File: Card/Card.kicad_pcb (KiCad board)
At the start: 2 copper layers, 89 x 51 mm, 4 parts

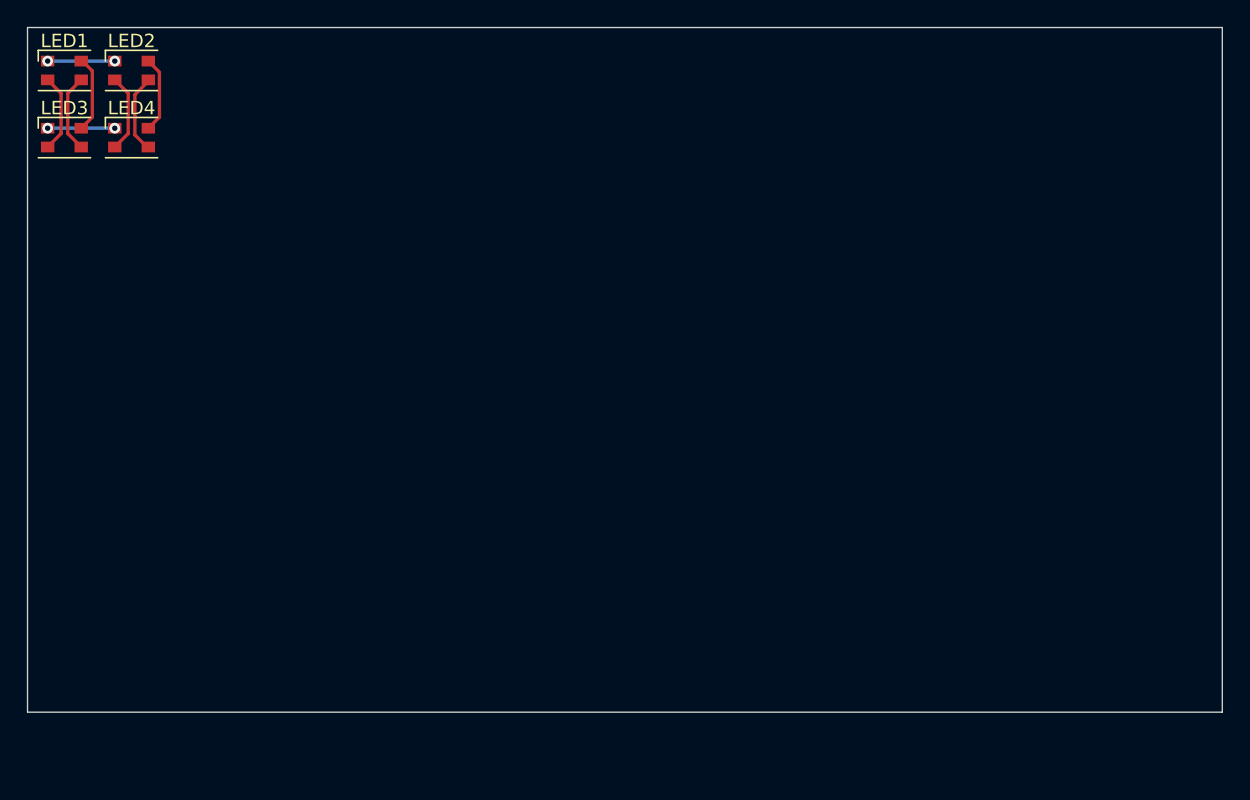
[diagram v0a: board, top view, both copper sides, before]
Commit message: Updated to UK card size
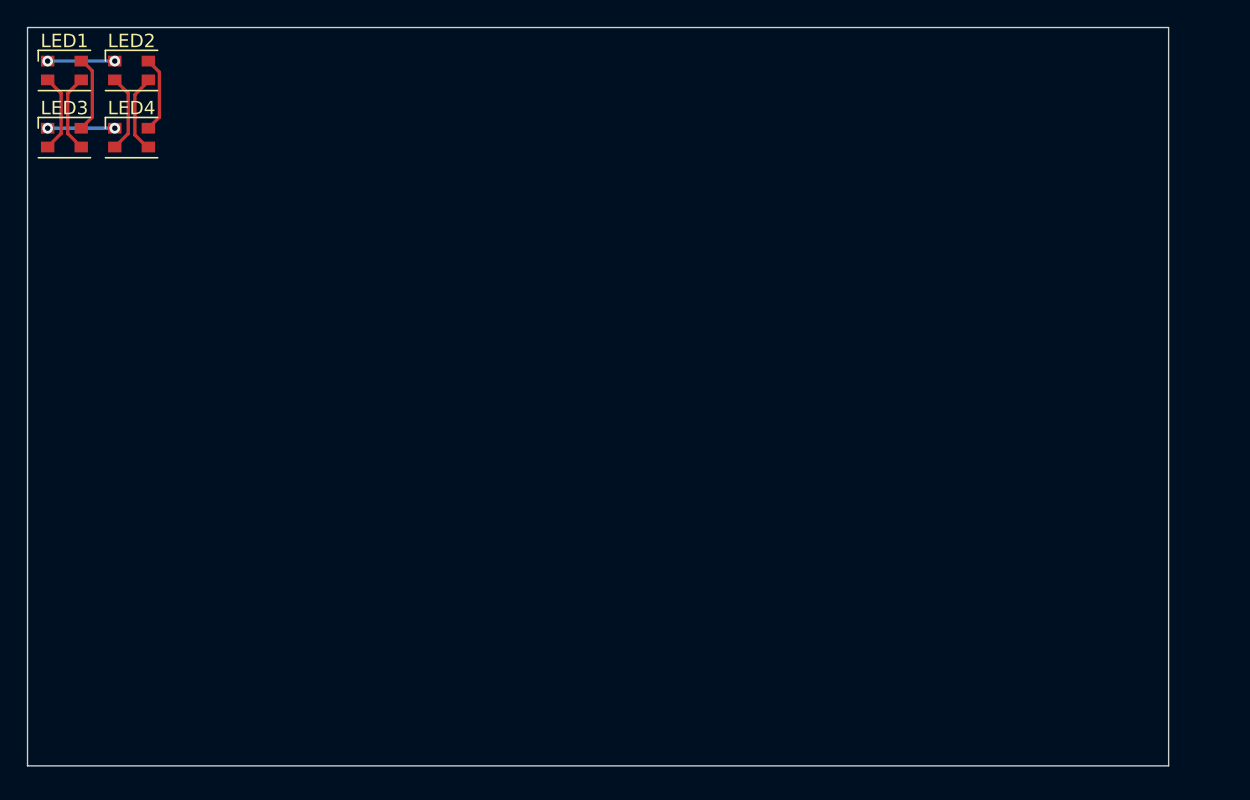
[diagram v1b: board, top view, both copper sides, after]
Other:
- board size 89 x 51 mm -> 85 x 55 mm
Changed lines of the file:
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@@
     )
   )
-  (gr_rect (start 100.5 61.5) (end 189.5 112.5)
+  (gr_rect (start 100.5 61.5) (end 185.5 116.5)
     (stroke (width 0.1) (type default)) (fill none) (layer "Edge.Cuts"))
   (via (at 107 64) (size 0.8) (drill 0.4) (layers "F.Cu" "B.Cu") (net 1))

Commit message: created LED matrix
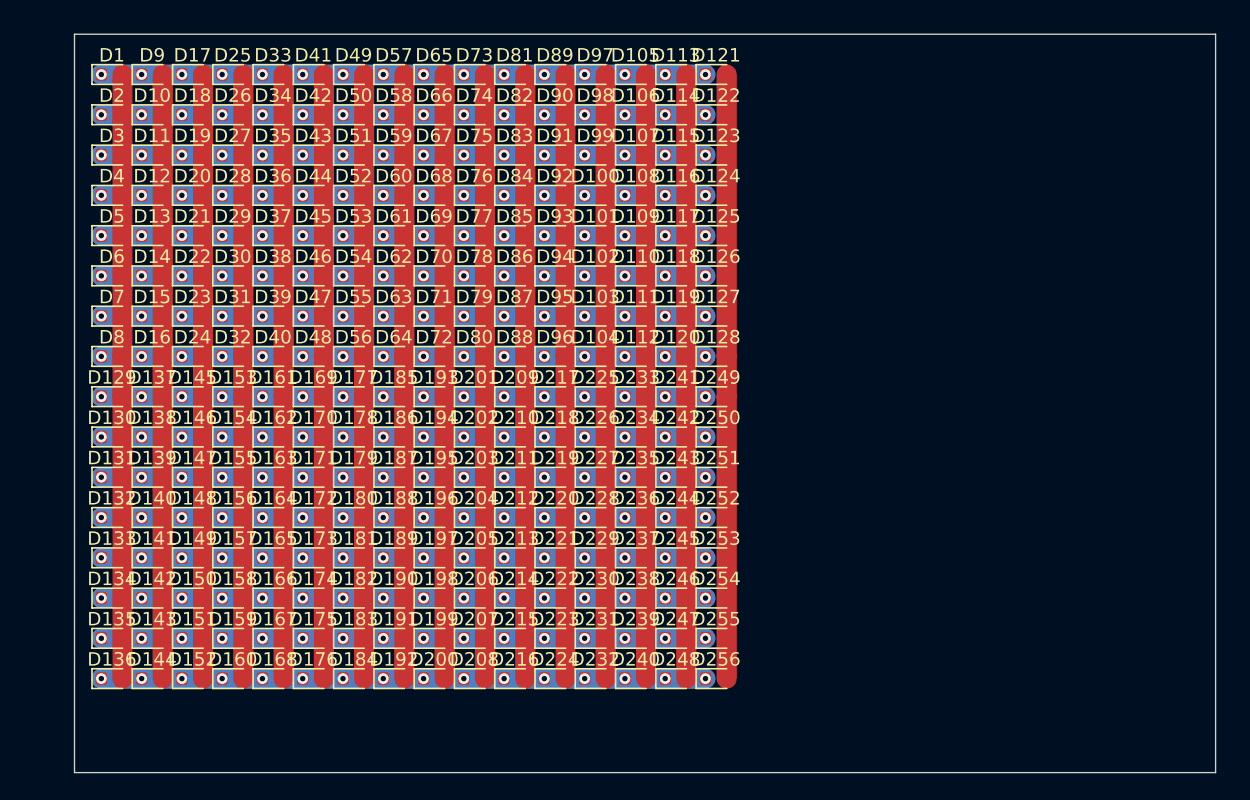
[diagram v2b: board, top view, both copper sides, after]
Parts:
- removed LED1, LED2, LED3, LED4: Tri-LED_CA, Footprints:LED_Cree-PLCC4_3.2x2.8mm_CCW
- added D1: LED, LED_SMD:LED_0603_1608Metric, F.Cu at (106.8, 65.0)
- added D10: LED, LED_SMD:LED_0603_1608Metric, F.Cu at (109.8, 68.0)
- added D100: LED, LED_SMD:LED_0603_1608Metric, F.Cu at (142.8, 74.0)
- added D101: LED, LED_SMD:LED_0603_1608Metric, F.Cu at (142.8, 77.0)
- added D102: LED, LED_SMD:LED_0603_1608Metric, F.Cu at (142.8, 80.0)
- added D103: LED, LED_SMD:LED_0603_1608Metric, F.Cu at (142.8, 83.0)
- added D104: LED, LED_SMD:LED_0603_1608Metric, F.Cu at (142.8, 86.0)
- added D105: LED, LED_SMD:LED_0603_1608Metric, F.Cu at (145.8, 65.0)
- added D106: LED, LED_SMD:LED_0603_1608Metric, F.Cu at (145.8, 68.0)
- added D107: LED, LED_SMD:LED_0603_1608Metric, F.Cu at (145.8, 71.0)
- added D108: LED, LED_SMD:LED_0603_1608Metric, F.Cu at (145.8, 74.0)
- added D109: LED, LED_SMD:LED_0603_1608Metric, F.Cu at (145.8, 77.0)
- added D11: LED, LED_SMD:LED_0603_1608Metric, F.Cu at (109.8, 71.0)
- added D110: LED, LED_SMD:LED_0603_1608Metric, F.Cu at (145.8, 80.0)
- added D111: LED, LED_SMD:LED_0603_1608Metric, F.Cu at (145.8, 83.0)
- added D112: LED, LED_SMD:LED_0603_1608Metric, F.Cu at (145.8, 86.0)
- added D113: LED, LED_SMD:LED_0603_1608Metric, F.Cu at (148.8, 65.0)
- added D114: LED, LED_SMD:LED_0603_1608Metric, F.Cu at (148.8, 68.0)
- added D115: LED, LED_SMD:LED_0603_1608Metric, F.Cu at (148.8, 71.0)
- added D116: LED, LED_SMD:LED_0603_1608Metric, F.Cu at (148.8, 74.0)
- added D117: LED, LED_SMD:LED_0603_1608Metric, F.Cu at (148.8, 77.0)
- added D118: LED, LED_SMD:LED_0603_1608Metric, F.Cu at (148.8, 80.0)
- added D119: LED, LED_SMD:LED_0603_1608Metric, F.Cu at (148.8, 83.0)
- added D12: LED, LED_SMD:LED_0603_1608Metric, F.Cu at (109.8, 74.0)
- added D120: LED, LED_SMD:LED_0603_1608Metric, F.Cu at (148.8, 86.0)
- added D121: LED, LED_SMD:LED_0603_1608Metric, F.Cu at (151.8, 65.0)
- added D122: LED, LED_SMD:LED_0603_1608Metric, F.Cu at (151.8, 68.0)
- added D123: LED, LED_SMD:LED_0603_1608Metric, F.Cu at (151.8, 71.0)
- added D124: LED, LED_SMD:LED_0603_1608Metric, F.Cu at (151.8, 74.0)
- added D125: LED, LED_SMD:LED_0603_1608Metric, F.Cu at (151.8, 77.0)
- added D126: LED, LED_SMD:LED_0603_1608Metric, F.Cu at (151.8, 80.0)
- added D127: LED, LED_SMD:LED_0603_1608Metric, F.Cu at (151.8, 83.0)
- added D128: LED, LED_SMD:LED_0603_1608Metric, F.Cu at (151.8, 86.0)
- added D129: LED, LED_SMD:LED_0603_1608Metric, F.Cu at (106.8, 89.0)
- added D13: LED, LED_SMD:LED_0603_1608Metric, F.Cu at (109.8, 77.0)
- added D130: LED, LED_SMD:LED_0603_1608Metric, F.Cu at (106.8, 92.0)
- added D131: LED, LED_SMD:LED_0603_1608Metric, F.Cu at (106.8, 95.0)
- added D132: LED, LED_SMD:LED_0603_1608Metric, F.Cu at (106.8, 98.0)
- added D133: LED, LED_SMD:LED_0603_1608Metric, F.Cu at (106.8, 101.0)
- added D134: LED, LED_SMD:LED_0603_1608Metric, F.Cu at (106.8, 104.0)
- added D135: LED, LED_SMD:LED_0603_1608Metric, F.Cu at (106.8, 107.0)
- added D136: LED, LED_SMD:LED_0603_1608Metric, F.Cu at (106.8, 110.0)
- added D137: LED, LED_SMD:LED_0603_1608Metric, F.Cu at (109.8, 89.0)
- added D138: LED, LED_SMD:LED_0603_1608Metric, F.Cu at (109.8, 92.0)
- added D139: LED, LED_SMD:LED_0603_1608Metric, F.Cu at (109.8, 95.0)
- added D14: LED, LED_SMD:LED_0603_1608Metric, F.Cu at (109.8, 80.0)
- added D140: LED, LED_SMD:LED_0603_1608Metric, F.Cu at (109.8, 98.0)
- added D141: LED, LED_SMD:LED_0603_1608Metric, F.Cu at (109.8, 101.0)
- added D142: LED, LED_SMD:LED_0603_1608Metric, F.Cu at (109.8, 104.0)
- added D143: LED, LED_SMD:LED_0603_1608Metric, F.Cu at (109.8, 107.0)
- added D144: LED, LED_SMD:LED_0603_1608Metric, F.Cu at (109.8, 110.0)
- added D145: LED, LED_SMD:LED_0603_1608Metric, F.Cu at (112.8, 89.0)
- added D146: LED, LED_SMD:LED_0603_1608Metric, F.Cu at (112.8, 92.0)
- added D147: LED, LED_SMD:LED_0603_1608Metric, F.Cu at (112.8, 95.0)
- added D148: LED, LED_SMD:LED_0603_1608Metric, F.Cu at (112.8, 98.0)
- added D149: LED, LED_SMD:LED_0603_1608Metric, F.Cu at (112.8, 101.0)
- added D15: LED, LED_SMD:LED_0603_1608Metric, F.Cu at (109.8, 83.0)
- added D150: LED, LED_SMD:LED_0603_1608Metric, F.Cu at (112.8, 104.0)
- added D151: LED, LED_SMD:LED_0603_1608Metric, F.Cu at (112.8, 107.0)
- added D152: LED, LED_SMD:LED_0603_1608Metric, F.Cu at (112.8, 110.0)
- added D153: LED, LED_SMD:LED_0603_1608Metric, F.Cu at (115.8, 89.0)
- added D154: LED, LED_SMD:LED_0603_1608Metric, F.Cu at (115.8, 92.0)
- added D155: LED, LED_SMD:LED_0603_1608Metric, F.Cu at (115.8, 95.0)
- added D156: LED, LED_SMD:LED_0603_1608Metric, F.Cu at (115.8, 98.0)
- added D157: LED, LED_SMD:LED_0603_1608Metric, F.Cu at (115.8, 101.0)
- added D158: LED, LED_SMD:LED_0603_1608Metric, F.Cu at (115.8, 104.0)
- added D159: LED, LED_SMD:LED_0603_1608Metric, F.Cu at (115.8, 107.0)
- added D16: LED, LED_SMD:LED_0603_1608Metric, F.Cu at (109.8, 86.0)
- added D160: LED, LED_SMD:LED_0603_1608Metric, F.Cu at (115.8, 110.0)
- added D161: LED, LED_SMD:LED_0603_1608Metric, F.Cu at (118.8, 89.0)
- added D162: LED, LED_SMD:LED_0603_1608Metric, F.Cu at (118.8, 92.0)
- added D163: LED, LED_SMD:LED_0603_1608Metric, F.Cu at (118.8, 95.0)
- added D164: LED, LED_SMD:LED_0603_1608Metric, F.Cu at (118.8, 98.0)
- added D165: LED, LED_SMD:LED_0603_1608Metric, F.Cu at (118.8, 101.0)
- added D166: LED, LED_SMD:LED_0603_1608Metric, F.Cu at (118.8, 104.0)
- added D167: LED, LED_SMD:LED_0603_1608Metric, F.Cu at (118.8, 107.0)
- added D168: LED, LED_SMD:LED_0603_1608Metric, F.Cu at (118.8, 110.0)
- added D169: LED, LED_SMD:LED_0603_1608Metric, F.Cu at (121.8, 89.0)
- added D17: LED, LED_SMD:LED_0603_1608Metric, F.Cu at (112.8, 65.0)
- added D170: LED, LED_SMD:LED_0603_1608Metric, F.Cu at (121.8, 92.0)
- added D171: LED, LED_SMD:LED_0603_1608Metric, F.Cu at (121.8, 95.0)
- added D172: LED, LED_SMD:LED_0603_1608Metric, F.Cu at (121.8, 98.0)
- added D173: LED, LED_SMD:LED_0603_1608Metric, F.Cu at (121.8, 101.0)
- added D174: LED, LED_SMD:LED_0603_1608Metric, F.Cu at (121.8, 104.0)
- added D175: LED, LED_SMD:LED_0603_1608Metric, F.Cu at (121.8, 107.0)
- added D176: LED, LED_SMD:LED_0603_1608Metric, F.Cu at (121.8, 110.0)
- added D177: LED, LED_SMD:LED_0603_1608Metric, F.Cu at (124.8, 89.0)
- added D178: LED, LED_SMD:LED_0603_1608Metric, F.Cu at (124.8, 92.0)
- added D179: LED, LED_SMD:LED_0603_1608Metric, F.Cu at (124.8, 95.0)
- added D18: LED, LED_SMD:LED_0603_1608Metric, F.Cu at (112.8, 68.0)
- added D180: LED, LED_SMD:LED_0603_1608Metric, F.Cu at (124.8, 98.0)
- added D181: LED, LED_SMD:LED_0603_1608Metric, F.Cu at (124.8, 101.0)
- added D182: LED, LED_SMD:LED_0603_1608Metric, F.Cu at (124.8, 104.0)
- added D183: LED, LED_SMD:LED_0603_1608Metric, F.Cu at (124.8, 107.0)
- added D184: LED, LED_SMD:LED_0603_1608Metric, F.Cu at (124.8, 110.0)
- added D185: LED, LED_SMD:LED_0603_1608Metric, F.Cu at (127.8, 89.0)
- added D186: LED, LED_SMD:LED_0603_1608Metric, F.Cu at (127.8, 92.0)
- added D187: LED, LED_SMD:LED_0603_1608Metric, F.Cu at (127.8, 95.0)
- added D188: LED, LED_SMD:LED_0603_1608Metric, F.Cu at (127.8, 98.0)
- added D189: LED, LED_SMD:LED_0603_1608Metric, F.Cu at (127.8, 101.0)
- added D19: LED, LED_SMD:LED_0603_1608Metric, F.Cu at (112.8, 71.0)
- added D190: LED, LED_SMD:LED_0603_1608Metric, F.Cu at (127.8, 104.0)
- added D191: LED, LED_SMD:LED_0603_1608Metric, F.Cu at (127.8, 107.0)
- added D192: LED, LED_SMD:LED_0603_1608Metric, F.Cu at (127.8, 110.0)
- added D193: LED, LED_SMD:LED_0603_1608Metric, F.Cu at (130.8, 89.0)
- added D194: LED, LED_SMD:LED_0603_1608Metric, F.Cu at (130.8, 92.0)
- added D195: LED, LED_SMD:LED_0603_1608Metric, F.Cu at (130.8, 95.0)
- added D196: LED, LED_SMD:LED_0603_1608Metric, F.Cu at (130.8, 98.0)
- added D197: LED, LED_SMD:LED_0603_1608Metric, F.Cu at (130.8, 101.0)
- added D198: LED, LED_SMD:LED_0603_1608Metric, F.Cu at (130.8, 104.0)
- added D199: LED, LED_SMD:LED_0603_1608Metric, F.Cu at (130.8, 107.0)
- added D2: LED, LED_SMD:LED_0603_1608Metric, F.Cu at (106.8, 68.0)
- added D20: LED, LED_SMD:LED_0603_1608Metric, F.Cu at (112.8, 74.0)
- added D200: LED, LED_SMD:LED_0603_1608Metric, F.Cu at (130.8, 110.0)
- added D201: LED, LED_SMD:LED_0603_1608Metric, F.Cu at (133.8, 89.0)
- added D202: LED, LED_SMD:LED_0603_1608Metric, F.Cu at (133.8, 92.0)
- added D203: LED, LED_SMD:LED_0603_1608Metric, F.Cu at (133.8, 95.0)
- added D204: LED, LED_SMD:LED_0603_1608Metric, F.Cu at (133.8, 98.0)
- added D205: LED, LED_SMD:LED_0603_1608Metric, F.Cu at (133.8, 101.0)
- added D206: LED, LED_SMD:LED_0603_1608Metric, F.Cu at (133.8, 104.0)
- added D207: LED, LED_SMD:LED_0603_1608Metric, F.Cu at (133.8, 107.0)
- added D208: LED, LED_SMD:LED_0603_1608Metric, F.Cu at (133.8, 110.0)
- added D209: LED, LED_SMD:LED_0603_1608Metric, F.Cu at (136.8, 89.0)
- added D21: LED, LED_SMD:LED_0603_1608Metric, F.Cu at (112.8, 77.0)
- added D210: LED, LED_SMD:LED_0603_1608Metric, F.Cu at (136.8, 92.0)
- added D211: LED, LED_SMD:LED_0603_1608Metric, F.Cu at (136.8, 95.0)
- added D212: LED, LED_SMD:LED_0603_1608Metric, F.Cu at (136.8, 98.0)
- added D213: LED, LED_SMD:LED_0603_1608Metric, F.Cu at (136.8, 101.0)
- added D214: LED, LED_SMD:LED_0603_1608Metric, F.Cu at (136.8, 104.0)
- added D215: LED, LED_SMD:LED_0603_1608Metric, F.Cu at (136.8, 107.0)
- added D216: LED, LED_SMD:LED_0603_1608Metric, F.Cu at (136.8, 110.0)
- added D217: LED, LED_SMD:LED_0603_1608Metric, F.Cu at (139.8, 89.0)
- added D218: LED, LED_SMD:LED_0603_1608Metric, F.Cu at (139.8, 92.0)
- added D219: LED, LED_SMD:LED_0603_1608Metric, F.Cu at (139.8, 95.0)
- added D22: LED, LED_SMD:LED_0603_1608Metric, F.Cu at (112.8, 80.0)
- added D220: LED, LED_SMD:LED_0603_1608Metric, F.Cu at (139.8, 98.0)
- added D221: LED, LED_SMD:LED_0603_1608Metric, F.Cu at (139.8, 101.0)
- added D222: LED, LED_SMD:LED_0603_1608Metric, F.Cu at (139.8, 104.0)
- added D223: LED, LED_SMD:LED_0603_1608Metric, F.Cu at (139.8, 107.0)
- added D224: LED, LED_SMD:LED_0603_1608Metric, F.Cu at (139.8, 110.0)
- added D225: LED, LED_SMD:LED_0603_1608Metric, F.Cu at (142.8, 89.0)
- added D226: LED, LED_SMD:LED_0603_1608Metric, F.Cu at (142.8, 92.0)
- added D227: LED, LED_SMD:LED_0603_1608Metric, F.Cu at (142.8, 95.0)
- added D228: LED, LED_SMD:LED_0603_1608Metric, F.Cu at (142.8, 98.0)
- added D229: LED, LED_SMD:LED_0603_1608Metric, F.Cu at (142.8, 101.0)
- added D23: LED, LED_SMD:LED_0603_1608Metric, F.Cu at (112.8, 83.0)
- added D230: LED, LED_SMD:LED_0603_1608Metric, F.Cu at (142.8, 104.0)
- added D231: LED, LED_SMD:LED_0603_1608Metric, F.Cu at (142.8, 107.0)
- added D232: LED, LED_SMD:LED_0603_1608Metric, F.Cu at (142.8, 110.0)
- added D233: LED, LED_SMD:LED_0603_1608Metric, F.Cu at (145.8, 89.0)
- added D234: LED, LED_SMD:LED_0603_1608Metric, F.Cu at (145.8, 92.0)
- added D235: LED, LED_SMD:LED_0603_1608Metric, F.Cu at (145.8, 95.0)
- added D236: LED, LED_SMD:LED_0603_1608Metric, F.Cu at (145.8, 98.0)
- added D237: LED, LED_SMD:LED_0603_1608Metric, F.Cu at (145.8, 101.0)
- added D238: LED, LED_SMD:LED_0603_1608Metric, F.Cu at (145.8, 104.0)
- added D239: LED, LED_SMD:LED_0603_1608Metric, F.Cu at (145.8, 107.0)
- added D24: LED, LED_SMD:LED_0603_1608Metric, F.Cu at (112.8, 86.0)
- added D240: LED, LED_SMD:LED_0603_1608Metric, F.Cu at (145.8, 110.0)
- added D241: LED, LED_SMD:LED_0603_1608Metric, F.Cu at (148.8, 89.0)
- added D242: LED, LED_SMD:LED_0603_1608Metric, F.Cu at (148.8, 92.0)
- added D243: LED, LED_SMD:LED_0603_1608Metric, F.Cu at (148.8, 95.0)
- added D244: LED, LED_SMD:LED_0603_1608Metric, F.Cu at (148.8, 98.0)
- added D245: LED, LED_SMD:LED_0603_1608Metric, F.Cu at (148.8, 101.0)
- added D246: LED, LED_SMD:LED_0603_1608Metric, F.Cu at (148.8, 104.0)
- added D247: LED, LED_SMD:LED_0603_1608Metric, F.Cu at (148.8, 107.0)
- added D248: LED, LED_SMD:LED_0603_1608Metric, F.Cu at (148.8, 110.0)
- added D249: LED, LED_SMD:LED_0603_1608Metric, F.Cu at (151.8, 89.0)
- added D25: LED, LED_SMD:LED_0603_1608Metric, F.Cu at (115.8, 65.0)
- added D250: LED, LED_SMD:LED_0603_1608Metric, F.Cu at (151.8, 92.0)
- added D251: LED, LED_SMD:LED_0603_1608Metric, F.Cu at (151.8, 95.0)
- added D252: LED, LED_SMD:LED_0603_1608Metric, F.Cu at (151.8, 98.0)
- added D253: LED, LED_SMD:LED_0603_1608Metric, F.Cu at (151.8, 101.0)
- added D254: LED, LED_SMD:LED_0603_1608Metric, F.Cu at (151.8, 104.0)
- added D255: LED, LED_SMD:LED_0603_1608Metric, F.Cu at (151.8, 107.0)
- added D256: LED, LED_SMD:LED_0603_1608Metric, F.Cu at (151.8, 110.0)
- added D26: LED, LED_SMD:LED_0603_1608Metric, F.Cu at (115.8, 68.0)
- added D27: LED, LED_SMD:LED_0603_1608Metric, F.Cu at (115.8, 71.0)
- added D28: LED, LED_SMD:LED_0603_1608Metric, F.Cu at (115.8, 74.0)
- added D29: LED, LED_SMD:LED_0603_1608Metric, F.Cu at (115.8, 77.0)
- added D3: LED, LED_SMD:LED_0603_1608Metric, F.Cu at (106.8, 71.0)
- added D30: LED, LED_SMD:LED_0603_1608Metric, F.Cu at (115.8, 80.0)
- added D31: LED, LED_SMD:LED_0603_1608Metric, F.Cu at (115.8, 83.0)
- added D32: LED, LED_SMD:LED_0603_1608Metric, F.Cu at (115.8, 86.0)
- added D33: LED, LED_SMD:LED_0603_1608Metric, F.Cu at (118.8, 65.0)
- added D34: LED, LED_SMD:LED_0603_1608Metric, F.Cu at (118.8, 68.0)
- added D35: LED, LED_SMD:LED_0603_1608Metric, F.Cu at (118.8, 71.0)
- added D36: LED, LED_SMD:LED_0603_1608Metric, F.Cu at (118.8, 74.0)
- added D37: LED, LED_SMD:LED_0603_1608Metric, F.Cu at (118.8, 77.0)
- added D38: LED, LED_SMD:LED_0603_1608Metric, F.Cu at (118.8, 80.0)
- added D39: LED, LED_SMD:LED_0603_1608Metric, F.Cu at (118.8, 83.0)
- added D4: LED, LED_SMD:LED_0603_1608Metric, F.Cu at (106.8, 74.0)
- added D40: LED, LED_SMD:LED_0603_1608Metric, F.Cu at (118.8, 86.0)
- added D41: LED, LED_SMD:LED_0603_1608Metric, F.Cu at (121.8, 65.0)
- added D42: LED, LED_SMD:LED_0603_1608Metric, F.Cu at (121.8, 68.0)
- added D43: LED, LED_SMD:LED_0603_1608Metric, F.Cu at (121.8, 71.0)
- added D44: LED, LED_SMD:LED_0603_1608Metric, F.Cu at (121.8, 74.0)
- added D45: LED, LED_SMD:LED_0603_1608Metric, F.Cu at (121.8, 77.0)
- added D46: LED, LED_SMD:LED_0603_1608Metric, F.Cu at (121.8, 80.0)
- added D47: LED, LED_SMD:LED_0603_1608Metric, F.Cu at (121.8, 83.0)
- added D48: LED, LED_SMD:LED_0603_1608Metric, F.Cu at (121.8, 86.0)
- added D49: LED, LED_SMD:LED_0603_1608Metric, F.Cu at (124.8, 65.0)
- added D5: LED, LED_SMD:LED_0603_1608Metric, F.Cu at (106.8, 77.0)
- added D50: LED, LED_SMD:LED_0603_1608Metric, F.Cu at (124.8, 68.0)
- added D51: LED, LED_SMD:LED_0603_1608Metric, F.Cu at (124.8, 71.0)
- added D52: LED, LED_SMD:LED_0603_1608Metric, F.Cu at (124.8, 74.0)
- added D53: LED, LED_SMD:LED_0603_1608Metric, F.Cu at (124.8, 77.0)
- added D54: LED, LED_SMD:LED_0603_1608Metric, F.Cu at (124.8, 80.0)
- added D55: LED, LED_SMD:LED_0603_1608Metric, F.Cu at (124.8, 83.0)
- added D56: LED, LED_SMD:LED_0603_1608Metric, F.Cu at (124.8, 86.0)
- added D57: LED, LED_SMD:LED_0603_1608Metric, F.Cu at (127.8, 65.0)
- added D58: LED, LED_SMD:LED_0603_1608Metric, F.Cu at (127.8, 68.0)
- added D59: LED, LED_SMD:LED_0603_1608Metric, F.Cu at (127.8, 71.0)
- added D6: LED, LED_SMD:LED_0603_1608Metric, F.Cu at (106.8, 80.0)
- added D60: LED, LED_SMD:LED_0603_1608Metric, F.Cu at (127.8, 74.0)
- added D61: LED, LED_SMD:LED_0603_1608Metric, F.Cu at (127.8, 77.0)
- added D62: LED, LED_SMD:LED_0603_1608Metric, F.Cu at (127.8, 80.0)
- added D63: LED, LED_SMD:LED_0603_1608Metric, F.Cu at (127.8, 83.0)
- added D64: LED, LED_SMD:LED_0603_1608Metric, F.Cu at (127.8, 86.0)
- added D65: LED, LED_SMD:LED_0603_1608Metric, F.Cu at (130.8, 65.0)
- added D66: LED, LED_SMD:LED_0603_1608Metric, F.Cu at (130.8, 68.0)
- added D67: LED, LED_SMD:LED_0603_1608Metric, F.Cu at (130.8, 71.0)
- added D68: LED, LED_SMD:LED_0603_1608Metric, F.Cu at (130.8, 74.0)
- added D69: LED, LED_SMD:LED_0603_1608Metric, F.Cu at (130.8, 77.0)
- added D7: LED, LED_SMD:LED_0603_1608Metric, F.Cu at (106.8, 83.0)
- added D70: LED, LED_SMD:LED_0603_1608Metric, F.Cu at (130.8, 80.0)
- added D71: LED, LED_SMD:LED_0603_1608Metric, F.Cu at (130.8, 83.0)
- added D72: LED, LED_SMD:LED_0603_1608Metric, F.Cu at (130.8, 86.0)
- added D73: LED, LED_SMD:LED_0603_1608Metric, F.Cu at (133.8, 65.0)
- added D74: LED, LED_SMD:LED_0603_1608Metric, F.Cu at (133.8, 68.0)
- added D75: LED, LED_SMD:LED_0603_1608Metric, F.Cu at (133.8, 71.0)
- added D76: LED, LED_SMD:LED_0603_1608Metric, F.Cu at (133.8, 74.0)
- added D77: LED, LED_SMD:LED_0603_1608Metric, F.Cu at (133.8, 77.0)
- added D78: LED, LED_SMD:LED_0603_1608Metric, F.Cu at (133.8, 80.0)
- added D79: LED, LED_SMD:LED_0603_1608Metric, F.Cu at (133.8, 83.0)
- added D8: LED, LED_SMD:LED_0603_1608Metric, F.Cu at (106.8, 86.0)
- added D80: LED, LED_SMD:LED_0603_1608Metric, F.Cu at (133.8, 86.0)
- added D81: LED, LED_SMD:LED_0603_1608Metric, F.Cu at (136.8, 65.0)
- added D82: LED, LED_SMD:LED_0603_1608Metric, F.Cu at (136.8, 68.0)
- added D83: LED, LED_SMD:LED_0603_1608Metric, F.Cu at (136.8, 71.0)
- added D84: LED, LED_SMD:LED_0603_1608Metric, F.Cu at (136.8, 74.0)
- added D85: LED, LED_SMD:LED_0603_1608Metric, F.Cu at (136.8, 77.0)
- added D86: LED, LED_SMD:LED_0603_1608Metric, F.Cu at (136.8, 80.0)
- added D87: LED, LED_SMD:LED_0603_1608Metric, F.Cu at (136.8, 83.0)
- added D88: LED, LED_SMD:LED_0603_1608Metric, F.Cu at (136.8, 86.0)
- added D89: LED, LED_SMD:LED_0603_1608Metric, F.Cu at (139.8, 65.0)
- added D9: LED, LED_SMD:LED_0603_1608Metric, F.Cu at (109.8, 65.0)
- added D90: LED, LED_SMD:LED_0603_1608Metric, F.Cu at (139.8, 68.0)
- added D91: LED, LED_SMD:LED_0603_1608Metric, F.Cu at (139.8, 71.0)
- added D92: LED, LED_SMD:LED_0603_1608Metric, F.Cu at (139.8, 74.0)
- added D93: LED, LED_SMD:LED_0603_1608Metric, F.Cu at (139.8, 77.0)
- added D94: LED, LED_SMD:LED_0603_1608Metric, F.Cu at (139.8, 80.0)
- added D95: LED, LED_SMD:LED_0603_1608Metric, F.Cu at (139.8, 83.0)
- added D96: LED, LED_SMD:LED_0603_1608Metric, F.Cu at (139.8, 86.0)
- added D97: LED, LED_SMD:LED_0603_1608Metric, F.Cu at (142.8, 65.0)
- added D98: LED, LED_SMD:LED_0603_1608Metric, F.Cu at (142.8, 68.0)
- added D99: LED, LED_SMD:LED_0603_1608Metric, F.Cu at (142.8, 71.0)
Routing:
- net /R9: track 0.00 -> 45.0 mm, vias 0 -> 16
- net /R8: track 0.00 -> 45.0 mm, vias 0 -> 16
- net /R7: track 0.00 -> 45.0 mm, vias 0 -> 16
- net /R6: track 0.00 -> 45.0 mm, vias 0 -> 16
- net /R5: track 0.00 -> 45.0 mm, vias 0 -> 16
- net /R4: track 0.00 -> 45.0 mm, vias 0 -> 16
- net /R3: track 0.00 -> 45.0 mm, vias 0 -> 16
- net /R2: track 0.00 -> 45.0 mm, vias 0 -> 16
- net /R15: track 0.00 -> 45.0 mm, vias 0 -> 16
- net /R14: track 0.00 -> 45.0 mm, vias 0 -> 16
- net /R13: track 0.00 -> 45.0 mm, vias 0 -> 16
- net /R12: track 0.00 -> 45.0 mm, vias 0 -> 16
- net /R11: track 0.00 -> 45.0 mm, vias 0 -> 16
- net /R10: track 0.00 -> 45.0 mm, vias 0 -> 16
- net /R1: track 0.00 -> 45.0 mm, vias 0 -> 16
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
